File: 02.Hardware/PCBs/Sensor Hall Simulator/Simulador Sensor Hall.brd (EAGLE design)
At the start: 78.5 x 44.8 mm, 29 parts

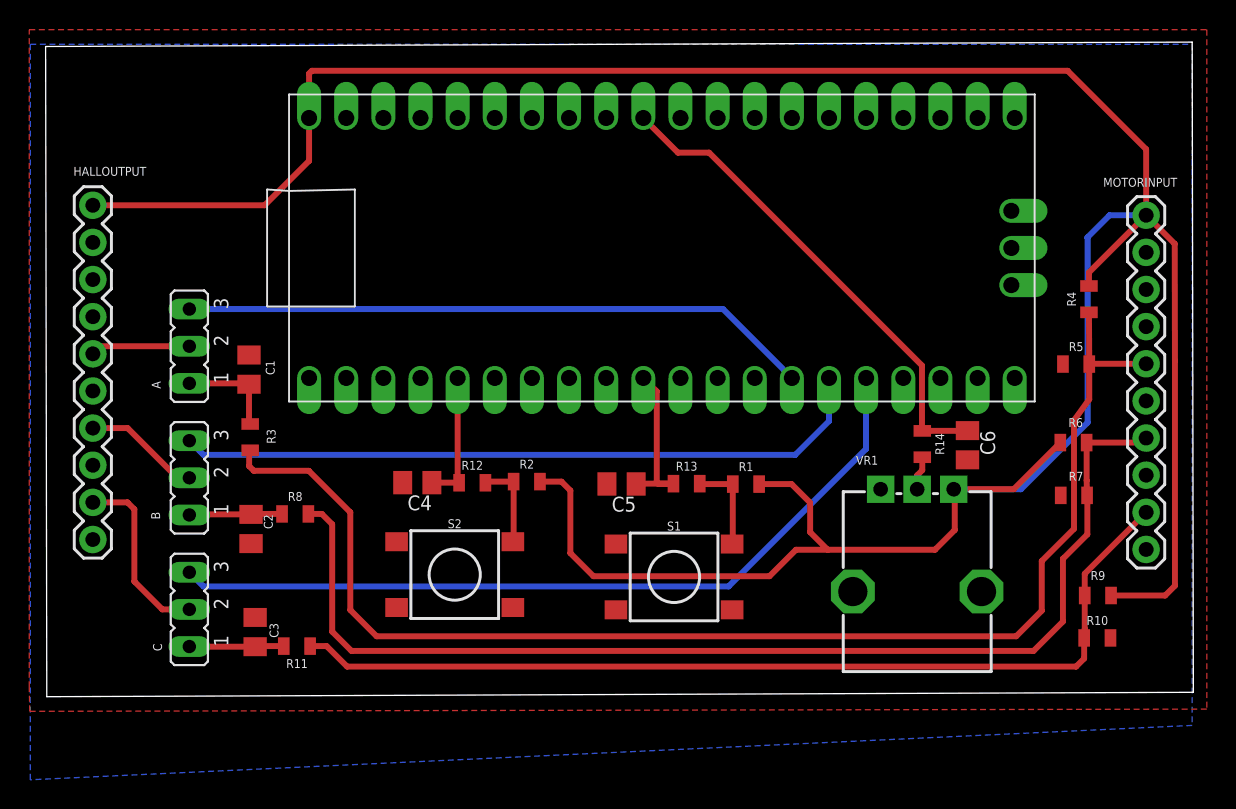
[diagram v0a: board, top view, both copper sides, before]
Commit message: v2 Simulador Sensor Hall
Eliminacion de conector de entrada sensores Hall.
Reduccion de tamaño.
Cambio del conector de entrada/salida
Correccion de errores
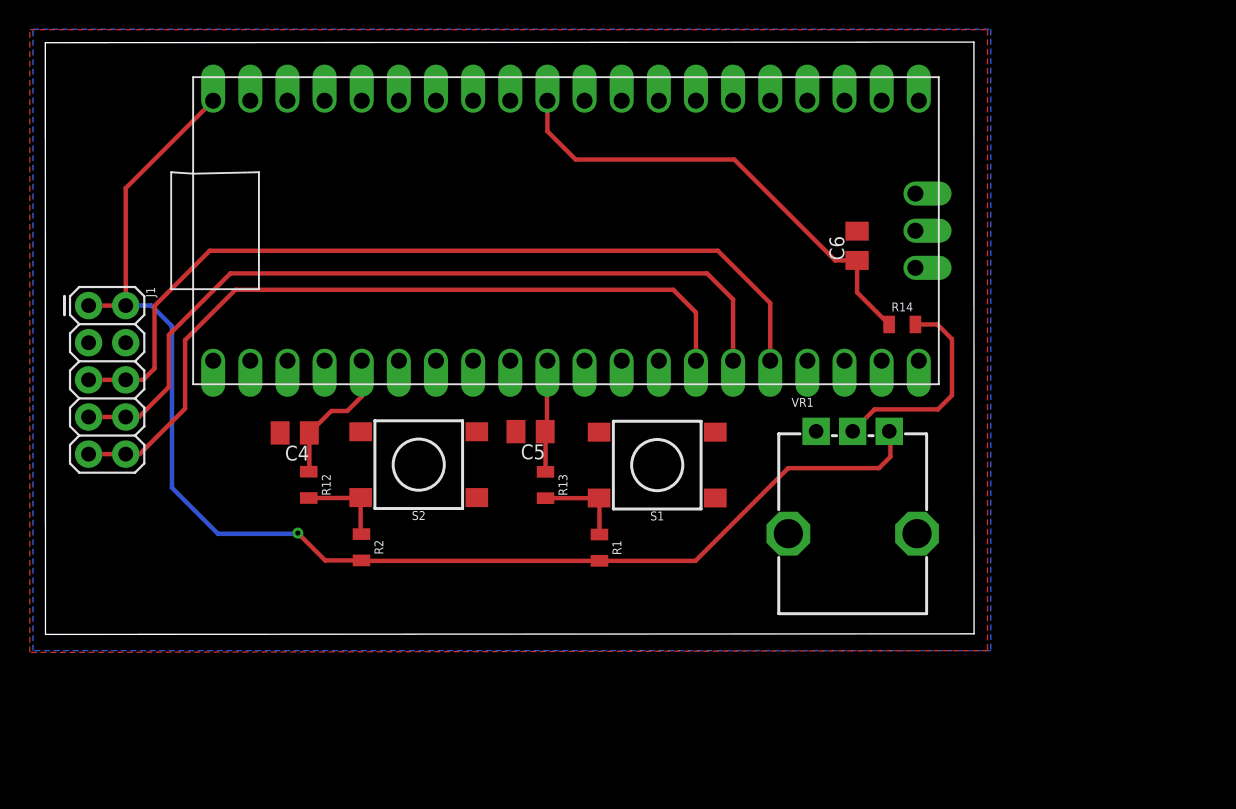
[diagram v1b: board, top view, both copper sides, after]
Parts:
- removed A, B, C: (no value), jumper:JP2
- removed C1, C2, C3: (no value), rcl:C0805K
- removed HALLOUTPUT, MOTORINPUT: (no value), SparkFun-Connectors:1X10
- removed R10, R11, R3, R4, R5, R6, R7, R8, R9: (no value), SparkFun-Resistors:0805
- added J1: (no value), SparkFun-Connectors:2X5
- moved C6 15.6 mm to (63.4, 30.7), turned to 90 degrees
- moved R2 12.2 mm to (29.5, 10.1), turned to 270 degrees
- moved R12 11.2 mm to (25.9, 14.3), turned to 270 degrees
- moved R1 10.9 mm to (45.7, 10.0), turned to 270 degrees
- moved R13 9.65 mm to (42.0, 14.3), turned to 270 degrees
- moved C4 9.04 mm to (24.9, 17.9)
- moved R14 8.29 mm to (66.5, 25.3), turned to 0 degrees
- moved S2 7.91 mm to (33.4, 15.7), turned to 180 degrees
- moved S1 7.74 mm to (49.7, 15.7), turned to 180 degrees
- moved C5 7.18 mm to (41.0, 18.0)
- moved X1 6.67 mm to (43.5, 31.7)
- moved VR1 5.93 mm to (63.1, 11.0)
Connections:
- removed net HALL_A_IN: A.1, C1.1, R3.2
- removed net HALL_A_OUT: A.2, HALLOUTPUT.6
- removed net HALL_A_SIM: A.3, X1.GP10
- removed net HALL_B_IN: B.1, C2.1, R8.1
- removed net HALL_B_OUT: B.2, HALLOUTPUT.4
- removed net HALL_B_SIM: B.3, X1.GP11
- removed net HALL_C_IN: C.1, C3.1, R11.2
- removed net HALL_C_OUT: C.2, HALLOUTPUT.2
- removed net HALL_C_SIM: C.3, X1.GP12
- removed net N$1: MOTORINPUT.6, R3.1, R4.1, R5.2
- removed net N$2: MOTORINPUT.4, R6.1, R7.2, R8.2
- removed net N$3: MOTORINPUT.2, R10.1, R11.1, R9.2
- new net HALL_A: J1.5, J1.6, X1.GP12
- new net HALL_B: J1.7, J1.8, X1.GP11
- new net HALL_C: J1.10, J1.9, X1.GP10
- net GND: now also J1.3, J1.4; no longer C1.2, C2.2, C3.2, HALLOUTPUT.8, MOTORINPUT.8, R10.2, R5.1, R7.1
- net VCC: now also J1.1, J1.2; no longer HALLOUTPUT.10, MOTORINPUT.10, R4.2, R6.2, R9.1
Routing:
- net VCC: track 205.7 -> 89.8 mm, vias 0 -> 1
- net N$1: track 90.3 -> 0.00 mm
- net N$2: track 77.8 -> 0.00 mm
- net N$3: track 65.5 -> 0.00 mm
- net HALL_A: track 0.00 -> 58.2 mm
- net HALL_C_SIM: track 55.4 -> 0.00 mm
- net HALL_B: track 0.00 -> 55.2 mm
- net HALL_C: track 0.00 -> 52.9 mm
- net HALL_B_SIM: track 48.1 -> 0.00 mm
- net HALL_A_SIM: track 43.2 -> 0.00 mm
- net HALL_C_OUT: track 12.5 -> 0.00 mm
- net N$8: track 2.33 -> 14.6 mm
- net HALL_B_OUT: track 8.01 -> 0.00 mm
- net HALL_A_IN: track 6.86 -> 0.00 mm
- net HALL_A_OUT: track 6.82 -> 0.00 mm
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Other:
- board size 78.5 x 44.8 mm -> 63.5 x 40.5 mm
- board text added: "SimSensorHall v2-Sep22"
- board text removed: "SimSensorHall v1-Sep22"

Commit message: Cambios menores
Pistas a 0.6 y algunos cambios menores
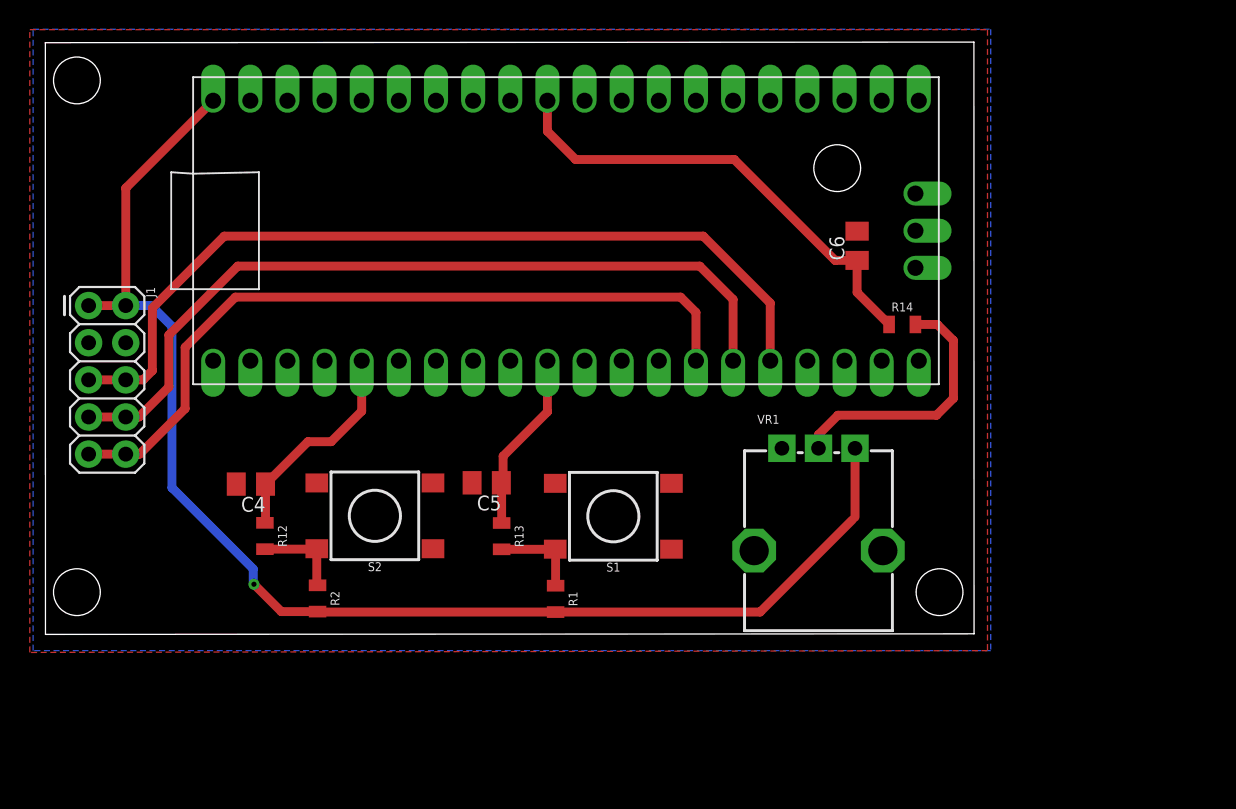
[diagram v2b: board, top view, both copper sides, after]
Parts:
- moved S2 4.61 mm to (30.4, 12.2)
- moved C4 4.61 mm to (21.9, 14.4)
- moved C5 4.61 mm to (38.0, 14.5)
- moved R12 4.61 mm to (22.9, 10.8)
- moved R13 4.61 mm to (39.0, 10.8)
- moved R2 4.61 mm to (26.5, 6.57)
- moved S1 4.61 mm to (46.7, 12.2)
- moved R1 4.61 mm to (42.7, 6.54)
- moved VR1 2.61 mm to (60.7, 9.84)
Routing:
- net START_STOP: track 9.73 -> 14.8 mm
- net DIR: track 7.67 -> 12.4 mm
- net N$8: track 14.6 -> 18.2 mm
- net VCC: track 89.8 -> 92.1 mm
- net HALL_A: track 58.2 -> 59.0 mm
- net HALL_C: track 52.9 -> 52.2 mm
